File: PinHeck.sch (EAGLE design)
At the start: 328 parts, among them IC1 FT232RL-REEL, IC2 PIC32MX795F512L-80I/PT, IC3 CD74HCT244E, IC4 CD74HCT244E, IC5 ULN2803A, J1 500075-1517, J11 No Load, J2 500075-1517, J3 N/A, J6 161-3507-E, P1 TC33X-2-103E, SW1 101-0134-EV, SW2 101-0134-EV, U1 P8X32A-Q44, U10 74HCT2G04GV,125, U11 74HC165D,652, U12 74HC165D,652, U14 MC74HC08ADG, U15 MC74HC08ADG, U16 MC74HC08ADG, U17 MC74HC08ADG, U18 MC74HC08ADG, U19 MC74HC08ADG, U2 FT230XS-R, U20 TIP107, U21 TIP107, U22 TIP107, U23 TIP107, U24 TIP107, U25 TIP107, U26 TIP107, U27 TIP107, U28 TIP102, U29 TIP102, U3 74HC595D-Q100, U30 TIP102, U31 TIP102, U32 TIP102, U33 TIP102, U34 TIP102, U35 TIP102, U36 WS2801, U37 TIP102, U38 WS2801, U39 LM2937IMP-3.3/NOPB, U4 24LC1025-I/P, U40 TIP102, U41 TIP102, U42 TIP102, U43 TIP102, U44 TIP102, U45 TIP102, U46 TIP102, U47 TIP102, U48 TIP102, U49 TIP102, U5 74HC595D-Q100, U50 TIP102, U51 TIP102, U52 CD74HC123M96, U6 TIP102, U7 TIP102, U8 TIP102, U9 TIP102, X1 FQ7050B-8.000, X2 ECS-65-20-4X

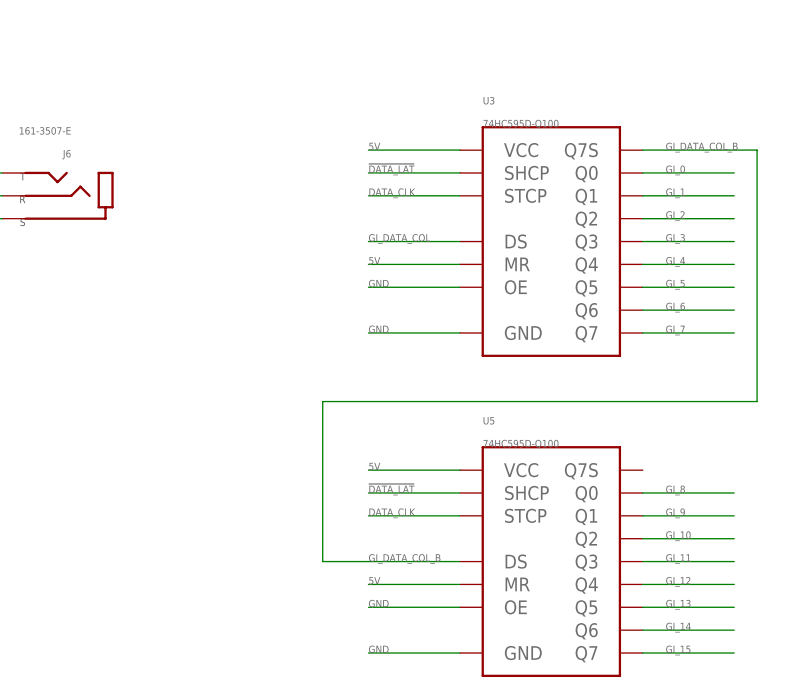
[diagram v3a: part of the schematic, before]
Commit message: Swapped LAT and CLK on 595. FIXED.
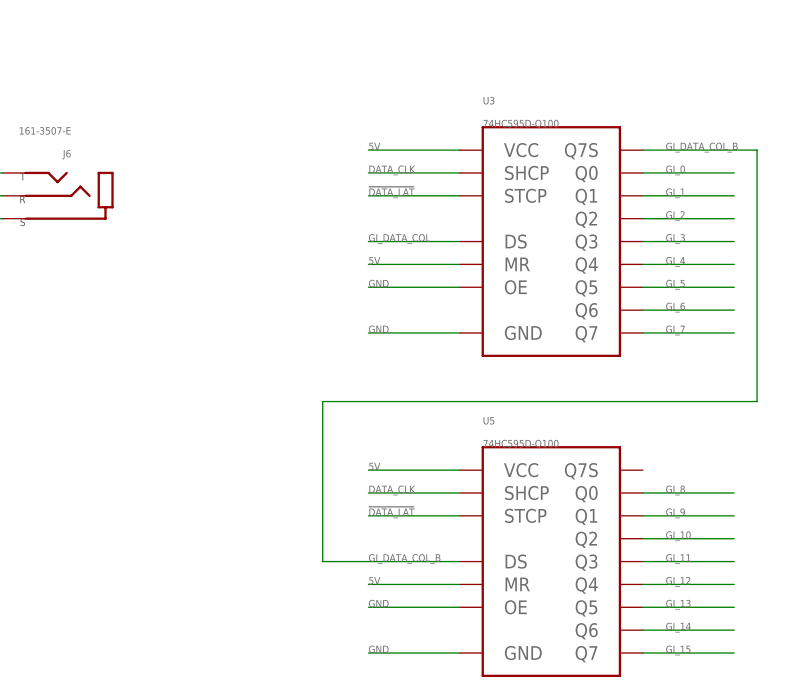
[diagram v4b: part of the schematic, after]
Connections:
- net !DATA_LAT: now also U3.STCP, U5.STCP; no longer U3.SHCP, U5.SHCP
- net DATA_CLK: now also U3.SHCP, U5.SHCP; no longer U3.STCP, U5.STCP
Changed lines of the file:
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@@
 <grid distance="0.1" unitdist="inch" unit="inch" style="lines" multiple="1" display="no" altdistance="0.01" altunitdist="inch" altunit="inch"/>
 <layers>
-<layer number="1" name="Top" color="4" fill="1" visible="yes" active="no"/>
-<layer number="2" name="Route2" color="1" fill="3" visible="yes" active="no"/>
-<layer number="3" name="Route3" color="4" fill="3" visible="yes" active="no"/>
-<layer number="4" name="Route4" color="1" fill="4" visible="yes" active="no"/>
-<layer number="5" name="Route5" color="4" fill="4" visible="yes" active="no"/>
-<layer number="6" name="Route6" color="1" fill="8" visible="yes" active="no"/>
-<layer number="7" name="Route7" color="4" fill="8" visible="yes" active="no"/>
-<layer number="8" name="Route8" color="1" fill="2" visible="yes" active="no"/>
-<layer number="9" name="Route9" color="4" fill="2" visible="yes" active="no"/>
-<layer number="10" name="Route10" color="1" fill="7" visible="yes" active="no"/>
-<layer number="11" name="Route11" color="4" fill="7" visible="yes" active="no"/>
-<layer number="12" name="Route12" color="1" fill="5" visible="yes" active="no"/>
-<layer number="13" name="Route13" color="4" fill="5" visible="yes" active="no"/>
-<layer number="14" name="Route14" color="1" fill="6" visible="yes" active="no"/>
-<layer number="15" name="Route15" color="4" fill="6" visible="yes" active="no"/>
-<layer number="16" name="Bottom" color="1" fill="1" visible="yes" active="no"/>
-<layer number="17" name="Pads" color="2" fill="1" visible="yes" active="no"/>
-<layer number="18" name="Vias" color="2" fill="1" visible="yes" active="no"/>
-<layer number="19" name="Unrouted" color="6" fill="1" visible="yes" active="no"/>
-<layer number="20" name="Dimension" color="15" fill="1" visible="yes" active="no"/>
-<layer number="21" name="tPlace" color="7" fill="1" visible="yes" active="no"/>
-<layer number="22" name="bPlace" color="7" fill="1" visible="yes" active="no"/>
-<layer number="23" name="tOrigins" color="15" fill="1" visible="yes" active="no"/>
-<layer number="24" name="bOrigins" color="15" fill="1" visible="yes" active="no"/>
-<layer number="25" name="tNames" color="7" fill="1" visible="yes" active="no"/>
-<layer number="26" name="bNames" color="7" fill="1" visible="yes" active="no"/>
-<layer number="27" name="tValues" color="7" fill="1" visible="yes" active="no"/>
-<layer number="28" name="bValues" color="7" fill="1" visible="yes" active="no"/>
+<layer number="1" name="Top" color="4" fill="1" visible="no" active="no"/>
+<layer number="2" name="Route2" color="1" fill="3" visible="no" active="no"/>
+<layer number="3" name="Route3" color="4" fill="3" visible="no" active="no"/>
+<layer number="4" name="Route4" color="1" fill="4" visible="no" active="no"/>
+<layer number="5" name="Route5" color="4" fill="4" visible="no" active="no"/>
+<layer number="6" name="Route6" color="1" fill="8" visible="no" active="no"/>
+<layer number="7" name="Route7" color="4" fill="8" visible="no" active="no"/>
+<layer number="8" name="Route8" color="1" fill="2" visible="no" active="no"/>
+<layer number="9" name="Route9" color="4" fill="2" visible="no" active="no"/>
+<layer number="10" name="Route10" color="1" fill="7" visible="no" active="no"/>
+<layer number="11" name="Route11" color="4" fill="7" visible="no" active="no"/>
+<layer number="12" name="Route12" color="1" fill="5" visible="no" active="no"/>
+<layer number="13" name="Route13" color="4" fill="5" visible="no" active="no"/>
+<layer number="14" name="Route14" color="1" fill="6" visible="no" active="no"/>
+<layer number="15" name="Route15" color="4" fill="6" visible="no" active="no"/>
+<layer number="16" name="Bottom" color="1" fill="1" visible="no" active="no"/>
+<layer number="17" name="Pads" color="2" fill="1" visible="no" active="no"/>
+<layer number="18" name="Vias" color="2" fill="1" visible="no" active="no"/>
+<layer number="19" name="Unrouted" color="6" fill="1" visible="no" active="no"/>
+<layer number="20" name="Dimension" color="15" fill="1" visible="no" active="no"/>
+<layer number="21" name="tPlace" color="7" fill="1" visible="no" active="no"/>
+<layer number="22" name="bPlace" color="7" fill="1" visible="no" active="no"/>
+<layer number="23" name="tOrigins" color="15" fill="1" visible="no" active="no"/>
+<layer number="24" name="bOrigins" color="15" fill="1" visible="no" active="no"/>
+<layer number="25" name="tNames" color="7" fill="1" visible="no" active="no"/>
+<layer number="26" name="bNames" color="7" fill="1" visible="no" active="no"/>
+<layer number="27" name="tValues" color="7" fill="1" visible="no" active="no"/>
+<layer number="28" name="bValues" color="7" fill="1" visible="no" active="no"/>
 <layer number="29" name="tStop" color="7" fill="3" visible="no" active="no"/>
 <layer number="30" name="bStop" color="7" fill="6" visible="no" active="no"/>
@@
 <layer number="35" name="tGlue" color="7" fill="4" visible="no" active="no"/>
 <layer number="36" name="bGlue" color="7" fill="5" visible="no" active="no"/>
-<layer number="37" name="tTest" color="7" fill="1" visible="yes" active="no"/>
-<layer number="38" name="bTest" color="7" fill="1" visible="yes" active="no"/>
+<layer number="37" name="tTest" color="7" fill="1" visible="no" active="no"/>
+<layer number="38" name="bTest" color="7" fill="1" visible="no" active="no"/>
 <layer number="39" name="tKeepout" color="4" fill="11" visible="no" active="no"/>
 <layer number="40" name="bKeepout" color="1" fill="11" visible="no" active="no"/>
@@
 <layer number="44" name="Drills" color="7" fill="1" visible="no" active="no"/>
 <layer number="45" name="Holes" color="7" fill="1" visible="no" active="no"/>
-<layer number="46" name="Milling" color="3" fill="1" visible="yes" active="no"/>
-<layer number="47" name="Measures" color="7" fill="1" visible="yes" active="no"/>
-<layer number="48" name="Document" color="7" fill="1" visible="yes" active="no"/>
-<layer number="49" name="Reference" color="7" fill="1" visible="yes" active="no"/>
-<layer number="50" name="dxf" color="7" fill="1" visible="yes" active="no"/>
-<layer number="51" name="tDocu" color="7" fill="1" visible="yes" active="no"/>
-<layer number="52" name="bDocu" color="7" fill="1" visible="yes" active="no"/>
-<layer number="53" name="tGND_GNDA" color="7" fill="9" visible="yes" active="no"/>
-<layer number="54" name="bGND_GNDA" color="1" fill="9" visible="yes" active="no"/>
-<layer number="56" name="wert" color="7" fill="1" visible="yes" active="no"/>
+<layer number="46" name="Milling" color="3" fill="1" visible="no" active="no"/>
+<layer number="47" name="Measures" color="7" fill="1" visible="no" active="no"/>
+<layer number="48" name="Document" color="7" fill="1" visible="no" active="no"/>
+<layer number="49" name="Reference" color="7" fill="1" visible="no" active="no"/>
+<layer number="50" name="dxf" color="7" fill="1" visible="no" active="no"/>
+<layer number="51" name="tDocu" color="7" fill="1" visible="no" active="no"/>
+<layer number="52" name="bDocu" color="7" fill="1" visible="no" active="no"/>
+<layer number="53" name="tGND_GNDA" color="7" fill="9" visible="no" active="no"/>
+<layer number="54" name="bGND_GNDA" color="1" fill="9" visible="no" active="no"/>
+<layer number="56" name="wert" color="7" fill="1" visible="no" active="no"/>
 <layer number="91" name="Nets" color="2" fill="1" visible="yes" active="yes"/>
 <layer number="92" name="Busses" color="1" fill="1" visible="yes" active="yes"/>
@@
 <net name="DATA_CLK" class="0">
 <segment>
-<pinref part="U3" gate="G$1" pin="STCP"/>
-<wire x1="330.2" y1="30.48" x2="320.04" y2="30.48" width="0.1524" layer="91"/>
-<label x="320.04" y="30.48" size="0.8128" layer="95" font="vector"/>
-</segment>
-<segment>
-<pinref part="U5" gate="G$1" pin="STCP"/>
-<wire x1="330.2" y1="-5.08" x2="320.04" y2="-5.08" width="0.1524" layer="91"/>
-<label x="320.04" y="-5.08" size="0.8128" layer="95" font="vector"/>
-</segment>
-<segment>
 <wire x1="276.86" y1="177.8" x2="292.1" y2="177.8" width="0.1524" layer="91"/>
 <label x="287.02" y="177.8" size="0.8128" layer="95" font="vector"/>
@@
 <label x="419.1" y="68.58" size="0.8128" layer="95" font="vector"/>
 </segment>
+<segment>
+<pinref part="U5" gate="G$1" pin="SHCP"/>
+<wire x1="320.04" y1="-2.54" x2="330.2" y2="-2.54" width="0.1524" layer="91"/>
+<label x="320.04" y="-2.54" size="0.8128" layer="95" font="vector"/>
+</segment>
+<segment>
+<pinref part="U3" gate="G$1" pin="SHCP"/>
+<wire x1="320.04" y1="33.02" x2="330.2" y2="33.02" width="0.1524" layer="91"/>
+<label x="320.04" y="33.02" size="0.8128" layer="95" font="vector"/>
+</segment>
 </net>
 <net name="GI_DATA_COL_B" class="0">
@@
 </segment>
 <segment>
-<pinref part="U3" gate="G$1" pin="SHCP"/>
-<wire x1="320.04" y1="33.02" x2="330.2" y2="33.02" width="0.1524" layer="91"/>
-<label x="320.04" y="33.02" size="0.8128" layer="95" font="vector"/>
+<pinref part="U3" gate="G$1" pin="STCP"/>
+<wire x1="330.2" y1="30.48" x2="320.04" y2="30.48" width="0.1524" layer="91"/>
+<label x="320.04" y="30.48" size="0.8128" layer="95" font="vector"/>
 </segment>
 <segment>
-<pinref part="U5" gate="G$1" pin="SHCP"/>
-<wire x1="320.04" y1="-2.54" x2="330.2" y2="-2.54" width="0.1524" layer="91"/>
-<label x="320.04" y="-2.54" size="0.8128" layer="95" font="vector"/>
+<pinref part="U5" gate="G$1" pin="STCP"/>
+<wire x1="330.2" y1="-5.08" x2="320.04" y2="-5.08" width="0.1524" layer="91"/>
+<label x="320.04" y="-5.08" size="0.8128" layer="95" font="vector"/>
 </segment>
 </net>

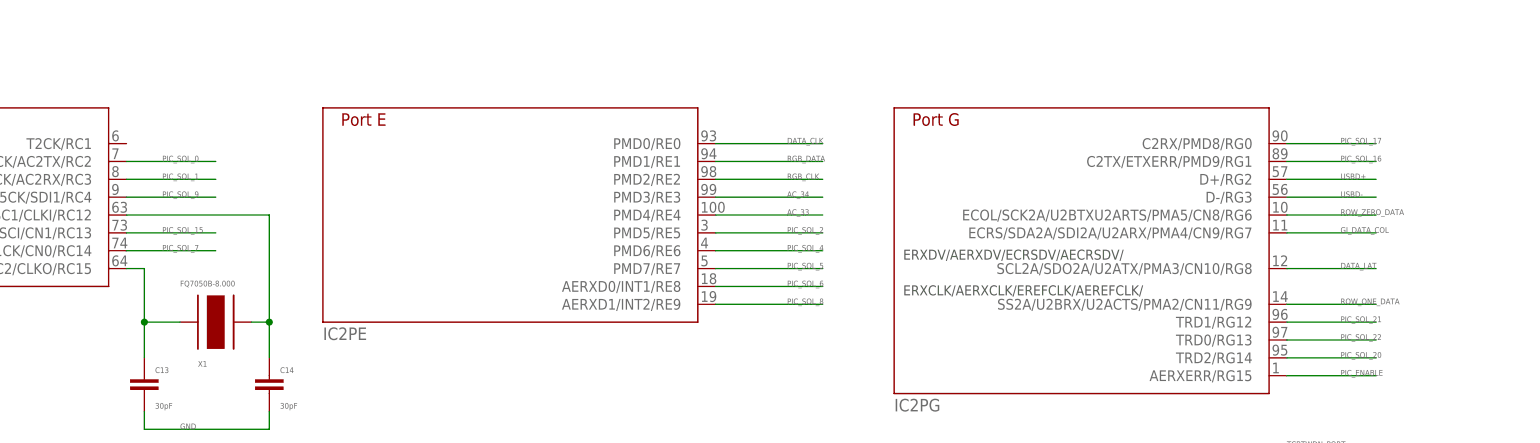
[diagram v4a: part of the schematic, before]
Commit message: Changed names for unused IO
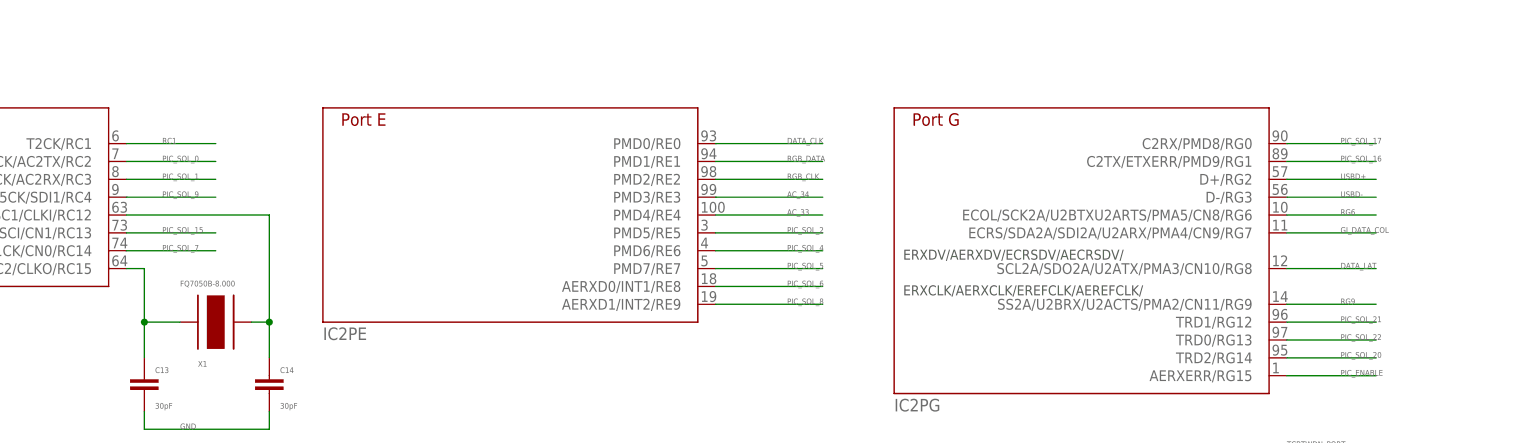
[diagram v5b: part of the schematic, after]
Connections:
- net ROW_ONE_DATA renamed RG9
- net ROW_ZERO_DATA renamed RG6
- new net RC1: IC2PC.T2CK/RC1
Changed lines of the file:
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@@
 <?xml version="1.0" encoding="utf-8"?>
 <!DOCTYPE eagle SYSTEM "eagle.dtd">
-<eagle version="6.5.0">
+<eagle version="6.3">
 <drawing>
 <settings>
@@
 </segment>
 </net>
-<net name="ROW_ZERO_DATA" class="0">
+<net name="RG6" class="0">
 <segment>
 <wire x1="358.14" y1="167.64" x2="370.84" y2="167.64" width="0.1524" layer="91"/>
@@
 </segment>
 </net>
-<net name="ROW_ONE_DATA" class="0">
+<net name="RG9" class="0">
 <segment>
 <wire x1="358.14" y1="154.94" x2="370.84" y2="154.94" width="0.1524" layer="91"/>
@@
 </segment>
 </net>
+<net name="RC1" class="0">
+<segment>
+<pinref part="IC2" gate="PC" pin="T2CK/RC1"/>
+<wire x1="193.04" y1="177.8" x2="205.74" y2="177.8" width="0.1524" layer="91"/>
+<label x="198.12" y="177.8" size="0.8128" layer="95" font="vector"/>
+</segment>
+</net>

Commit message: Added Bluetooth
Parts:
- added BT1: RN-41, PP_Sensors:RN-41RN-41
- added BT_RX, BT_TX, USBDM, USBDP, VBUS: (no value), PP_Connectors:PH_1X02HEADER_PTH
- added C28: .1uF, PP_Passives:CAPACITOR_NON_POLAR0805
- added C29: 10uF, PP_Passives:CAPACITOR_NON_POLAR1206
- added R137, R138, R139: 10K, PP_Passives:RESISTOR0805
- added SW3: 101-0134-EV, PP_Electromechanical:SPST101-0134-EV
- added SW4: 0S102011MS2QS1, PP_Electromechanical:SPDT0S102011MS2QS1
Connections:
- new net BT_RESET: BT1.RESET, R138.2, SW4.1
- new net BT_RX: BT1.UARTRX, BT_RX.1
- new net BT_TX: BT1.UARTTX, BT_TX.1
- new net FT232_RESET: IC1.RESET#, R139.1, SW4.3
- net 3.3V: now also BT1.VDD, C28.2, C29.1, R137.2, SW4.2
- net DM: now also USBDM.2
- net DP: now also USBDP.2
- net FT_3.3V: no longer IC1.RESET#
- net GND: now also BT1.GND, BT1.GND1, BT1.GND2, BT1.GND3, BT1.GND4, BT1.GND5, C28.1, C29.2, R138.1, R139.2, SW3.B
- net RG9: now also R137.1, SW3.A
- net RX_PIC32: now also BT_RX.2
- net TX_PIC32: now also BT_TX.2
- net USBD+: now also USBDP.1
- net USBD-: now also USBDM.1
- net USB_BUS: now also VBUS.2
- net VUSB: now also VBUS.1
